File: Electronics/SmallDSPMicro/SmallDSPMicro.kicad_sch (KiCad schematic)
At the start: 56 parts, among them J11 Programming, P1 USB_C_Plug_USB2.0, Q1 NSS1C300ET4G, Q2 2N7002, SW2 TS-1187A-B-A-B, U1 ADAU1463, U2 ADM811, U3 M95M01-R, U7 CP2615-xx-xM, Y1 830105957509

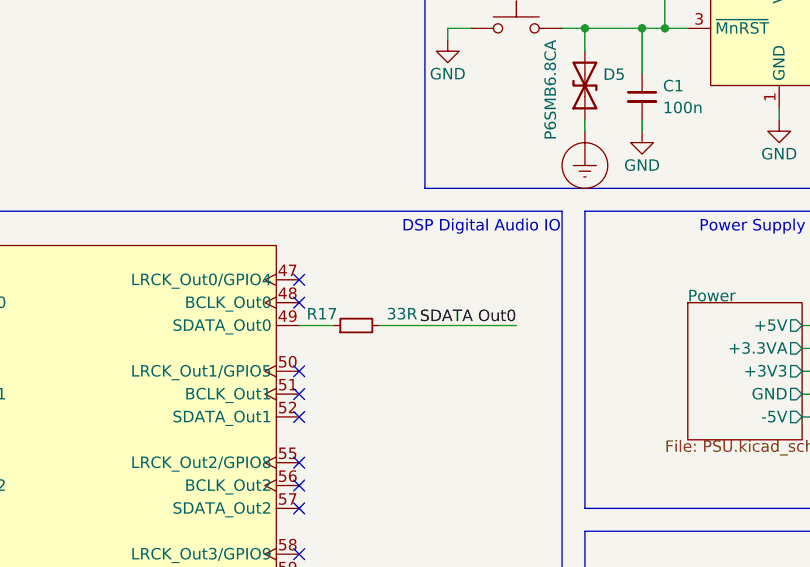
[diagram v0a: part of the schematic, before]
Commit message: Fixes wrong connection in maxi schematic
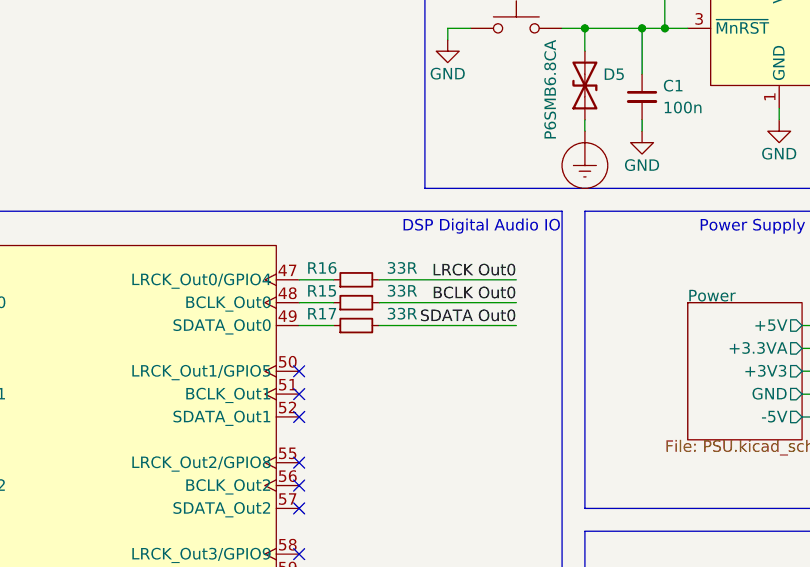
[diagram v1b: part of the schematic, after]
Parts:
- added R15, R16: 33R, Resistor_SMD:R_0402_1005Metric, symbol Device:R_Small
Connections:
- net at U1.47 (LRCK_Out0/GPIO4): now also R16.1
- net at U1.48 (BCLK_Out0): now also R15.1
- new net BCLK Out0: R15.2
- new net LRCK Out0: R16.2
- no-connect marks 49 -> 47
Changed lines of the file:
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@@
   (no_connect (at 93.98 88.9))
   (no_connect (at 96.52 154.94))
-  (no_connect (at 144.78 66.04))
   (no_connect (at 144.78 86.36))
   (no_connect (at 96.52 147.32))
@@
   (no_connect (at 93.98 116.84))
   (no_connect (at 93.98 99.06))
-  (no_connect (at 144.78 63.5))
   (no_connect (at 93.98 76.2))
   (no_connect (at 142.24 175.26))
@@
     (stroke (width 0) (type default))
   )
+  (wire (pts (xy 153.67 66.04) (xy 168.91 66.04))
+    (stroke (width 0) (type default))
+  )
   (wire (pts (xy 224.79 109.22) (xy 224.79 110.49))
     (stroke (width 0) (type default))
@@
     (stroke (width 0) (type default))
   )
+  (wire (pts (xy 153.67 63.5) (xy 168.91 63.5))
+    (stroke (width 0) (type default))
+  )
   (wire (pts (xy 245.11 74.93) (xy 234.95 74.93))
     (stroke (width 0) (type default))
@@
     (stroke (width 0) (type default))
   )
+  (wire (pts (xy 144.78 63.5) (xy 148.59 63.5))
+    (stroke (width 0) (type default))
+  )
   (wire (pts (xy 194.31 130.81) (xy 204.47 130.81))
     (stroke (width 0) (type default))
@@
     (stroke (width 0) (type default))
   )
+  (wire (pts (xy 144.78 66.04) (xy 148.59 66.04))
+    (stroke (width 0) (type default))
+  )
   (wire (pts (xy 262.89 132.08) (xy 262.89 135.89))
     (stroke (width 0) (type default))
@@
     (effects (font (size 1.27 1.27)) (justify right bottom))
   )
+  (label "BCLK Out0" (at 168.91 66.04 180) (fields_autoplaced)
+    (effects (font (size 1.27 1.27)) (justify right bottom))
+  )
   (label "M DSP MOSI" (at 232.41 64.77 0) (fields_autoplaced)
     (effects (font (size 1.27 1.27)) (justify left bottom))
@@
     (effects (font (size 1.27 1.27)) (justify right bottom))
   )
+  (label "LRCK Out0" (at 168.91 63.5 180) (fields_autoplaced)
+    (effects (font (size 1.27 1.27)) (justify right bottom))
+  )
   (label "SDATA In0" (at 72.39 68.58 0) (fields_autoplaced)
     (effects (font (size 1.27 1.27)) (justify left bottom))
@@
     )
   )
+  (symbol (lib_id "Device:R_Small") (at 151.13 66.04 90) (unit 1)
+    (in_bom yes) (on_board yes) (dnp no)
+    (property "Reference" "R15" (at 147.32 64.77 90)
+      (effects (font (size 1.27 1.27)))
+    )
+    (property "Value" "33R" (at 156.21 64.77 90)
+      (effects (font (size 1.27 1.27)))
+    )
+    (property "Footprint" "Resistor_SMD:R_0402_1005Metric" (at 151.13 66.04 0)
+      (effects (font (size 1.27 1.27)) hide)
+    )
+    (property "Datasheet" "~" (at 151.13 66.04 0)
+      (effects (font (size 1.27 1.27)) hide)
+    )
+    (property "Dielectric" "" (at 151.13 66.04 0)
+      (effects (font (size 1.27 1.27)) hide)
+    )
+    (property "Notes" "" (at 151.13 66.04 0)
+      (effects (font (size 1.27 1.27)) hide)
+    )
+    (property "Rated Voltage" "" (at 151.13 66.04 0)
+      (effects (font (size 1.27 1.27)) hide)
+    )
+    (property "Assembling" "X" (at 151.13 66.04 0)
+      (effects (font (size 1.27 1.27)) hide)
+    )
+    (property "Manufacturer" "UNI-ROYAL(Uniroyal Elec)" (at 151.13 66.04 0)
+      (effects (font (size 1.27 1.27)) hide)
+    )
+    (property "Part Number" "0402WGF330JTCE" (at 151.13 66.04 0)
+      (effects (font (size 1.27 1.27)) hide)
+    )
+    (property "Rated Power" "62.5mW" (at 151.13 66.04 0)
+      (effects (font (size 1.27 1.27)) hide)
+    )
+    (property "Rated Current" "" (at 151.13 66.04 0)
+      (effects (font (size 1.27 1.27)) hide)
+    )
+    (property "Tolerance" "1%" (at 151.13 66.04 0)
+      (effects (font (size 1.27 1.27)) hide)
+    )
+    (property "LCSC Part #" "C25105" (at 151.13 66.04 0)
+      (effects (font (size 1.27 1.27)) hide)
+    )
+    (pin "1")
+    (pin "2")
+    (instances
+      (project "SmallDSPMicro"
+        (path "/5f2729b5-edcd-4fbc-b3fb-44096724c941"
+          (reference "R15") (unit 1)
+        )
+      )
+    )
+  )
   (symbol (lib_id "power:+3V3") (at 209.55 119.38 0) (unit 1)
     (in_bom yes) (on_board yes) (dnp no)
@@
         )
       )
+    )
+  )
+  (symbol (lib_id "Device:R_Small") (at 151.13 63.5 90) (unit 1)
+    (in_bom yes) (on_board yes) (dnp no)
+    (property "Reference" "R16" (at 147.32 62.23 90)
+      (effects (font (size 1.27 1.27)))
+    )
+    (property "Value" "33R" (at 156.21 62.23 90)
+      (effects (font (size 1.27 1.27)))
+    )
+    (property "Footprint" "Resistor_SMD:R_0402_1005Metric" (at 151.13 63.5 0)
+      (effects (font (size 1.27 1.27)) hide)
+    )
+    (property "Datasheet" "~" (at 151.13 63.5 0)
+      (effects (font (size 1.27 1.27)) hide)
+    )
+    (property "Dielectric" "" (at 151.13 63.5 0)
+      (effects (font (size 1.27 1.27)) hide)
+    )
+    (property "Notes" "" (at 151.13 63.5 0)
+      (effects (font (size 1.27 1.27)) hide)
+    )
+    (property "Rated Voltage" "" (at 151.13 63.5 0)
+      (effects (font (size 1.27 1.27)) hide)
+    )
+    (property "Assembling" "X" (at 151.13 63.5 0)
+      (effects (font (size 1.27 1.27)) hide)
+    )
+    (property "Manufacturer" "UNI-ROYAL(Uniroyal Elec)" (at 151.13 63.5 0)
+      (effects (font (size 1.27 1.27)) hide)
+    )
+    (property "Part Number" "0402WGF330JTCE" (at 151.13 63.5 0)
+      (effects (font (size 1.27 1.27)) hide)
+    )
+    (property "Rated Power" "62.5mW" (at 151.13 63.5 0)
+      (effects (font (size 1.27 1.27)) hide)
+    )
+    (property "Rated Current" "" (at 151.13 63.5 0)
+      (effects (font (size 1.27 1.27)) hide)
+    )
+    (property "Tolerance" "1%" (at 151.13 63.5 0)
+      (effects (font (size 1.27 1.27)) hide)
+    )
+    (property "LCSC Part #" "C25105" (at 151.13 63.5 0)
+      (effects (font (size 1.27 1.27)) hide)
+    )
+    (pin "1")
+    (pin "2")
+    (instances
+      (project "SmallDSPMicro"
+        (path "/5f2729b5-edcd-4fbc-b3fb-44096724c941"
+          (reference "R16") (unit 1)
+        )
+      )
